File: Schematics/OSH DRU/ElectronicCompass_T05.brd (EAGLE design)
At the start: 50.5 x 50.8 mm, 67 parts, among them Q1 FDN360P, Q2 FDN360P, Q3 FDN360P, Q4 FDN360P, Q5 BC817-16LT1SMD, Q6 BC817-16LT1SMD, U1 ATMEGA32U4, X1 USBSMD, Y1 16MHz

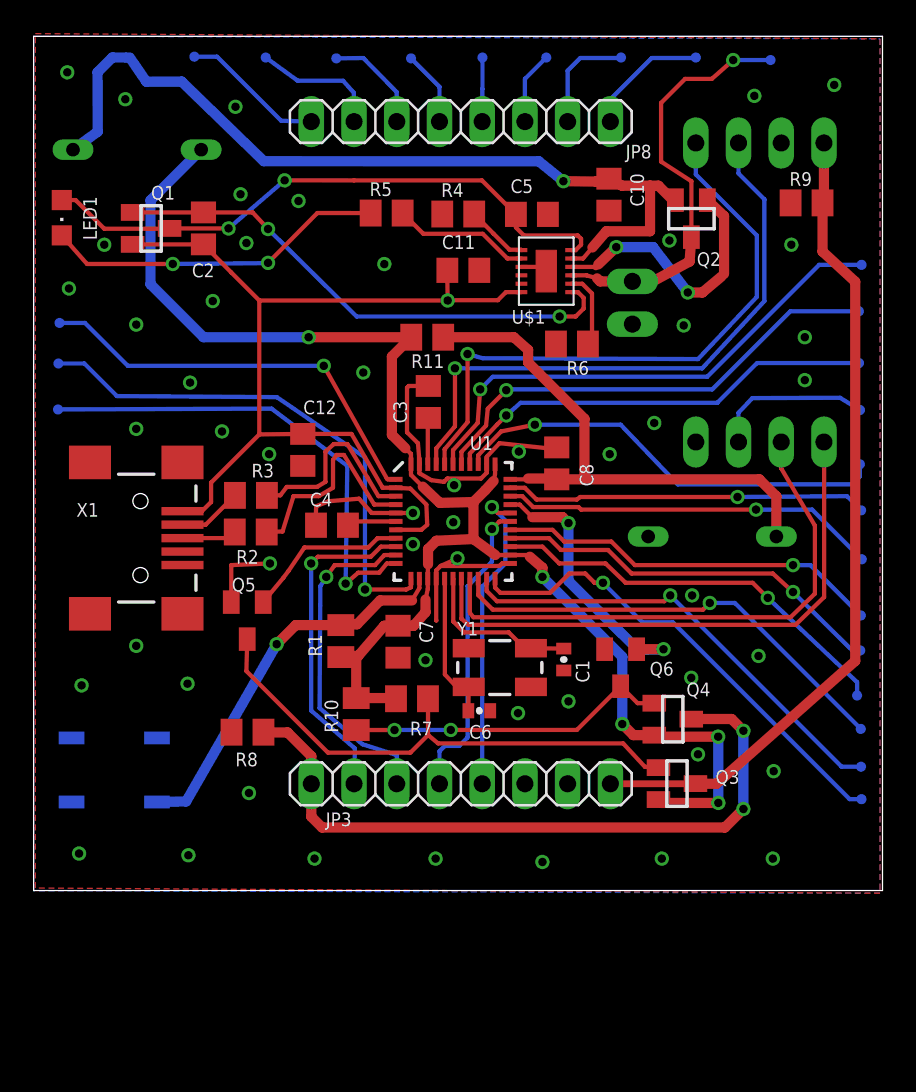
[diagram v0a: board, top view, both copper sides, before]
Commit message: Fixed PMIC pins and GPIO switches
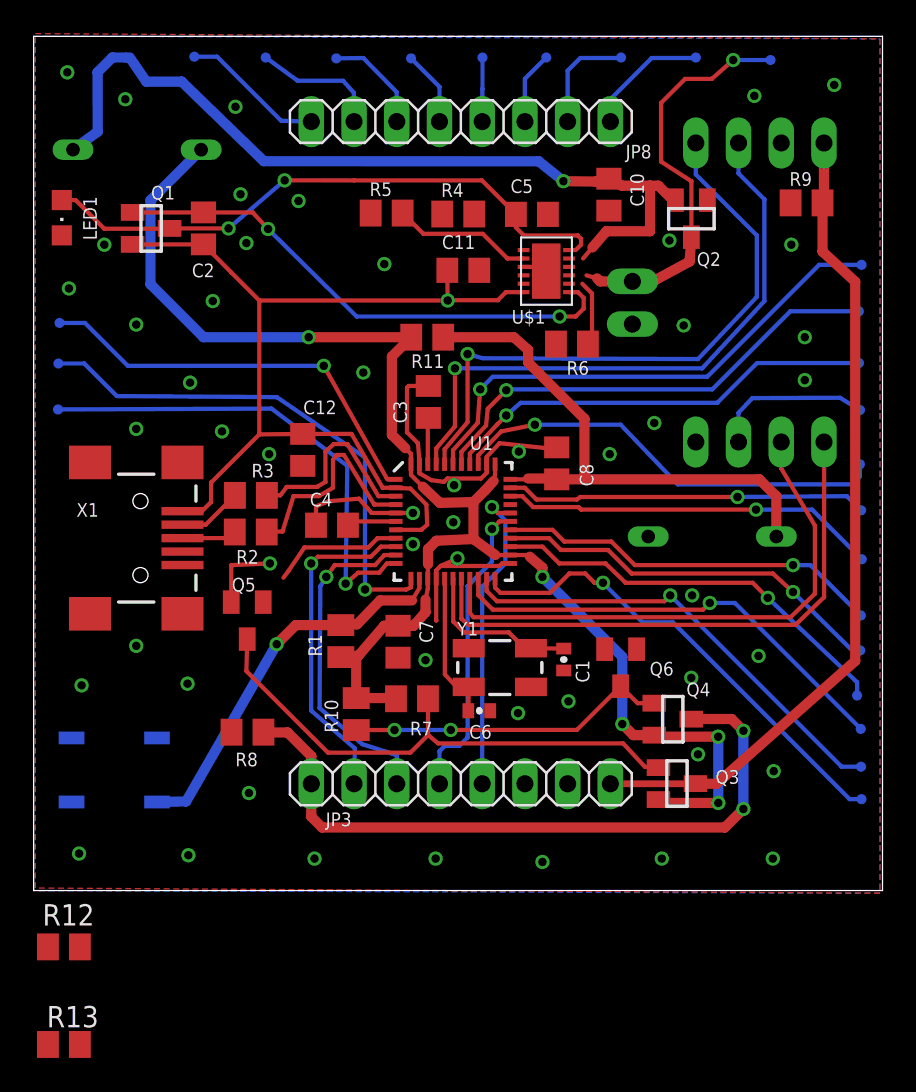
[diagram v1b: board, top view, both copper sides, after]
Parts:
- added R12: 1k, rcl:M0805
- added R13: 1k, resistor:M0805
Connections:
- new net N$46: Q2.1, U$1.P9
- new net N$47: Q5.B, R13.1
- net N$16: now also R12.2, U1.30; no longer Q2.1, U$1.P10
- net N$37: now also R13.2; no longer Q5.B
- net N$44: now also R12.1; no longer U1.30
- net N$5: now also U$1.P10; no longer U$1.P9
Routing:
- net N$8: track 20.4 -> 0.00 mm, vias 2 -> 0
- net N$16: track 16.3 -> 0.00 mm, vias 2 -> 0
- net N$44: track 16.3 -> 0.00 mm, vias 2 -> 0
- net N$4: track 3.70 -> 0.00 mm
- net N$37: track 9.74 -> 7.85 mm
- net N$5: track 25.4 -> 24.5 mm
- net N$36: track 51.6 -> 50.9 mm
- net N$1: track 4.59 -> 3.93 mm

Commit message: board layout complete
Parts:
- moved R12 42.2 mm to (40.6, 13.2), turned to 90 degrees
- moved R13 28.2 mm to (12.7, 16.9), turned to 90 degrees
- moved Q5 3.53 mm to (11.8, 12.7)
- moved JP4 1.20 mm to (36.5, 35.8)
- moved C5 0.35 mm to (30.0, 40.3)
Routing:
- net N$8: track 0.00 -> 22.8 mm, vias 0 -> 2
- net N$16: track 0.00 -> 17.9 mm, vias 0 -> 2
- net N$46: track 0.00 -> 17.6 mm
- net N$44: track 0.00 -> 6.66 mm
- net GND: track 38.4 -> 44.3 mm, vias 51 -> 56
- net N$4: track 0.00 -> 4.23 mm
- net D-: track 11.7 -> 8.35 mm
- net N$34: track 12.8 -> 9.63 mm
- net N$37: track 7.85 -> 10.3 mm
- net N$47: track 0.00 -> 2.20 mm
- net N$45: track 31.8 -> 30.5 mm
- net N$5: track 24.5 -> 25.4 mm
- net N$1: track 3.93 -> 4.63 mm
- net N$6: track 35.3 -> 36.0 mm
- net N$36: track 50.9 -> 51.5 mm
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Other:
- board text added: "1"

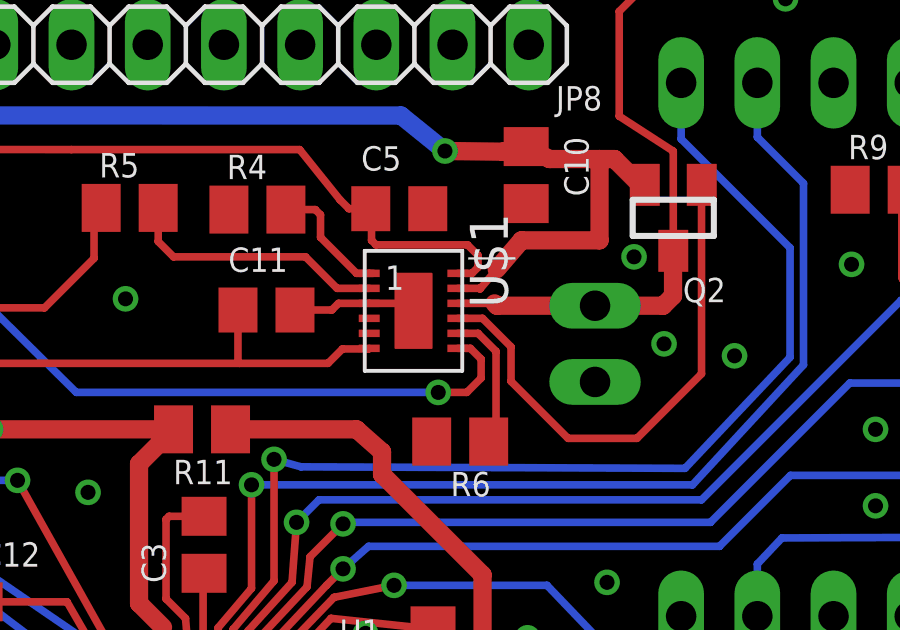
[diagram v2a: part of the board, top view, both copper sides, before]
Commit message: s-screen layout update
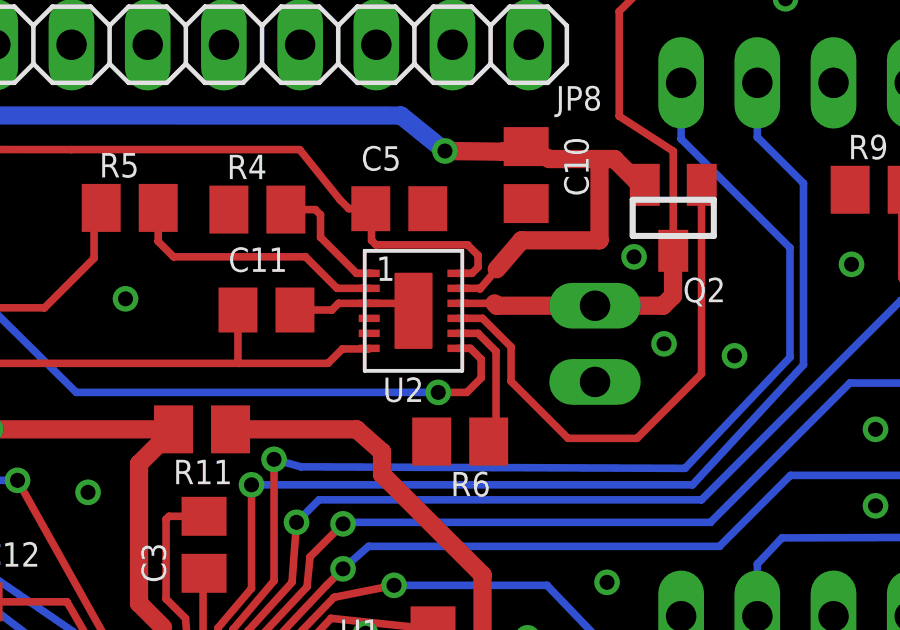
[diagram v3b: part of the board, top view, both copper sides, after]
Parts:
- renumbered U$1 to U2
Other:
- board text added: "PSU-Practicum-ECE 411-Fall 2013"
- board text removed: "PSU Practicum - ECE 411 Fall 2013"
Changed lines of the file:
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@@
 <grid distance="0.05" unitdist="mm" unit="mm" style="lines" multiple="1" display="yes" altdistance="0.00625" altunitdist="inch" altunit="mm"/>
 <layers>
-<layer number="1" name="Top" color="4" fill="1" visible="yes" active="yes"/>
+<layer number="1" name="Top" color="4" fill="1" visible="no" active="yes"/>
 <layer number="16" name="Bottom" color="1" fill="1" visible="yes" active="yes"/>
 <layer number="17" name="Pads" color="2" fill="1" visible="yes" active="yes"/>
@@
 <layer number="19" name="Unrouted" color="6" fill="1" visible="yes" active="yes"/>
 <layer number="20" name="Dimension" color="15" fill="1" visible="yes" active="yes"/>
-<layer number="21" name="tPlace" color="7" fill="1" visible="yes" active="yes"/>
+<layer number="21" name="tPlace" color="7" fill="1" visible="no" active="yes"/>
 <layer number="22" name="bPlace" color="7" fill="1" visible="yes" active="yes"/>
-<layer number="23" name="tOrigins" color="15" fill="1" visible="yes" active="yes"/>
+<layer number="23" name="tOrigins" color="15" fill="1" visible="no" active="yes"/>
 <layer number="24" name="bOrigins" color="15" fill="1" visible="yes" active="yes"/>
-<layer number="25" name="tNames" color="7" fill="1" visible="yes" active="yes"/>
+<layer number="25" name="tNames" color="7" fill="1" visible="no" active="yes"/>
 <layer number="26" name="bNames" color="7" fill="1" visible="yes" active="yes"/>
-<layer number="27" name="tValues" color="7" fill="1" visible="yes" active="yes"/>
+<layer number="27" name="tValues" color="7" fill="1" visible="no" active="yes"/>
 <layer number="28" name="bValues" color="7" fill="1" visible="yes" active="yes"/>
 <layer number="29" name="tStop" color="7" fill="3" visible="no" active="yes"/>
@@
 <layer number="37" name="tTest" color="7" fill="1" visible="no" active="yes"/>
 <layer number="38" name="bTest" color="7" fill="1" visible="no" active="yes"/>
-<layer number="39" name="tKeepout" color="4" fill="11" visible="yes" active="yes"/>
+<layer number="39" name="tKeepout" color="4" fill="11" visible="no" active="yes"/>
 <layer number="40" name="bKeepout" color="1" fill="11" visible="yes" active="yes"/>
-<layer number="41" name="tRestrict" color="4" fill="10" visible="yes" active="yes"/>
+<layer number="41" name="tRestrict" color="4" fill="10" visible="no" active="yes"/>
 <layer number="42" name="bRestrict" color="1" fill="10" visible="yes" active="yes"/>
 <layer number="43" name="vRestrict" color="2" fill="10" visible="yes" active="yes"/>
@@
 <layer number="49" name="Reference" color="7" fill="1" visible="yes" active="yes"/>
 <layer number="50" name="dxf" color="7" fill="1" visible="no" active="no"/>
-<layer number="51" name="tDocu" color="7" fill="1" visible="yes" active="yes"/>
+<layer number="51" name="tDocu" color="7" fill="1" visible="no" active="yes"/>
 <layer number="52" name="bDocu" color="7" fill="1" visible="yes" active="yes"/>
 <layer number="53" name="tGND_GNDA" color="7" fill="9" visible="no" active="no"/>
@@
 <wire x1="50.47" y1="50.79" x2="0" y2="50.79" width="0" layer="20"/>
 <wire x1="0" y1="50.79" x2="0" y2="0" width="0" layer="20"/>
-<text x="32.3" y="35.05" size="0.8128" layer="26" rot="MR0">Team 05 - Electronic Compass for Robot
+<text x="34.55" y="35" size="0.8128" layer="26" rot="MR0">Team 05 - Electronic Compass for Robot
 Benjamin Huntsman
 Michael Walton
 Cody Gabriel
 John Maseda</text>
-<text x="32.35" y="31.3" size="0.8128" layer="26" rot="MR0">PSU Practicum - ECE 411
-                          Fall 2013 </text>
-<text x="29.5" y="37.55" size="0.8128" layer="25">1</text>
+<text x="35.3" y="32.55" size="0.8128" layer="26" rot="MR0">PSU-Practicum-ECE 411-Fall 2013 </text>
+<text x="29.2" y="37.85" size="0.8128" layer="25">1</text>
 </plain>
 <attributes>
@@
 <attribute name="NAME" x="11.684" y="15.884" size="0.8128" layer="25" rot="R90"/>
 </element>
-<element name="U$1" library="LTC4067" package="DFN-12" value="LTC4067" x="30.45" y="36.85" rot="R270"/>
+<element name="U2" library="LTC4067" package="DFN-12" value="LTC4067" x="30.45" y="36.85" smashed="yes" rot="R270">
+<attribute name="NAME" x="30.8" y="34.625" size="0.8128" layer="25" rot="R180"/>
+</element>
 </elements>
 <signals>
@@
 <via x="15.3" y="17.15" extent="1-16" drill="0.5"/>
 <via x="14.95" y="10.4" extent="1-16" drill="0.5"/>
-<contactref element="U$1" pad="P13"/>
-<contactref element="U$1" pad="P5"/>
-<contactref element="U$1" pad="P4"/>
-<contactref element="U$1" pad="P3"/>
+<contactref element="U2" pad="P13"/>
+<contactref element="U2" pad="P5"/>
+<contactref element="U2" pad="P4"/>
+<contactref element="U2" pad="P3"/>
 <wire x1="28.973" y1="37.1" x2="30.2" y2="37.1" width="0.254" layer="1"/>
 <wire x1="30.2" y1="37.1" x2="30.45" y2="36.85" width="0.254" layer="1"/>
@@
 <wire x1="4.2" y1="39.35" x2="8.065" y2="39.35" width="0.254" layer="1"/>
 <wire x1="8.065" y1="39.35" x2="8.085" y2="39.37" width="0.254" layer="1"/>
-<contactref element="U$1" pad="P12"/>
+<contactref element="U2" pad="P12"/>
 <wire x1="31.927" y1="38.1" x2="32.4" y2="38.1" width="0.254" layer="1"/>
 <wire x1="32.4" y1="38.1" x2="32.6" y2="38.3" width="0.254" layer="1"/>
@@
 <wire x1="32.22625" y1="34.13125" x2="31.27375" y2="34.13125" width="0.254" layer="1"/>
 <wire x1="5.885" y1="40.32" x2="10.0975" y2="40.32" width="0.254" layer="1"/>
-<contactref element="U$1" pad="P7"/>
+<contactref element="U2" pad="P7"/>
 <wire x1="31.927" y1="35.6" x2="32.345" y2="35.6" width="0.254" layer="1"/>
 </signal>
@@
 <wire x1="18.9" y1="27.15" x2="20.75" y2="23.95" width="0.254" layer="1"/>
 <wire x1="21.535" y1="23.94875" x2="20.75" y2="23.95" width="0.254" layer="1"/>
-<contactref element="U$1" pad="P6"/>
+<contactref element="U2" pad="P6"/>
 <wire x1="27.6" y1="35.1" x2="24.65" y2="35.1" width="0.254" layer="1"/>
 <wire x1="24.65" y1="35.1" x2="13.4325" y2="35.1" width="0.254" layer="1"/>
@@
 <wire x1="39.1" y1="37.35" x2="39.1" y2="38.8425" width="0.6096" layer="1"/>
 <wire x1="39.1" y1="38.8425" x2="39.1075" y2="38.85" width="0.6096" layer="1"/>
-<contactref element="U$1" pad="P10"/>
+<contactref element="U2" pad="P10"/>
 <wire x1="31.927" y1="37.1" x2="33.15" y2="37.1" width="0.254" layer="1"/>
 </signal>
@@
 <wire x1="34.05" y1="39.2" x2="36.65" y2="39.2" width="0.6096" layer="1"/>
 <wire x1="36.65" y1="39.2" x2="36.65" y2="41.91" width="0.6096" layer="1"/>
-<contactref element="U$1" pad="P11"/>
+<contactref element="U2" pad="P11"/>
 <wire x1="31.927" y1="37.6" x2="32.6475" y2="37.6" width="0.254" layer="1"/>
 <wire x1="32.6475" y1="37.6" x2="32.6675" y2="37.58" width="0.254" layer="1"/>
@@
 <wire x1="33.2" y1="35.5" x2="33.2" y2="32.74" width="0.254" layer="1"/>
 <wire x1="33.2" y1="32.74" x2="32.955" y2="32.495" width="0.254" layer="1"/>
-<contactref element="U$1" pad="P8"/>
+<contactref element="U2" pad="P8"/>
 <wire x1="31.927" y1="36.1" x2="32.6" y2="36.1" width="0.254" layer="1"/>
 </signal>
@@
 <wire x1="27.35" y1="39.3" x2="28.55" y2="38.1" width="0.254" layer="1"/>
 <wire x1="28.55" y1="38.1" x2="28.973" y2="38.1" width="0.254" layer="1"/>
-<contactref element="U$1" pad="P1"/>
+<contactref element="U2" pad="P1"/>
 <wire x1="29.11" y1="38.1" x2="28.973" y2="38.1" width="0.254" layer="1"/>
 </signal>
@@
 <wire x1="40.05" y1="34.75" x2="40.05" y2="41.0425" width="0.254" layer="1"/>
 <wire x1="40.05" y1="41.0425" x2="40.0575" y2="41.05" width="0.254" layer="1"/>
-<contactref element="U$1" pad="P9"/>
+<contactref element="U2" pad="P9"/>
 <wire x1="31.927" y1="36.6" x2="32.75" y2="36.6" width="0.254" layer="1"/>
 </signal>
@@
 <signal name="N$7">
 <contactref element="R5" pad="2"/>
-<contactref element="U$1" pad="P2"/>
+<contactref element="U2" pad="P2"/>
 <wire x1="21.93875" y1="40.28125" x2="21.93875" y2="39.16125" width="0.254" layer="1"/>
 <wire x1="21.93875" y1="39.16125" x2="22.45" y2="38.65" width="0.254" layer="1"/>
